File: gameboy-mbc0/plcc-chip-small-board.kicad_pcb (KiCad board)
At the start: 2 copper layers, 49.5 x 30.8 mm, 2 parts, among them P1 CONN_01X32, U1 SST39SF010

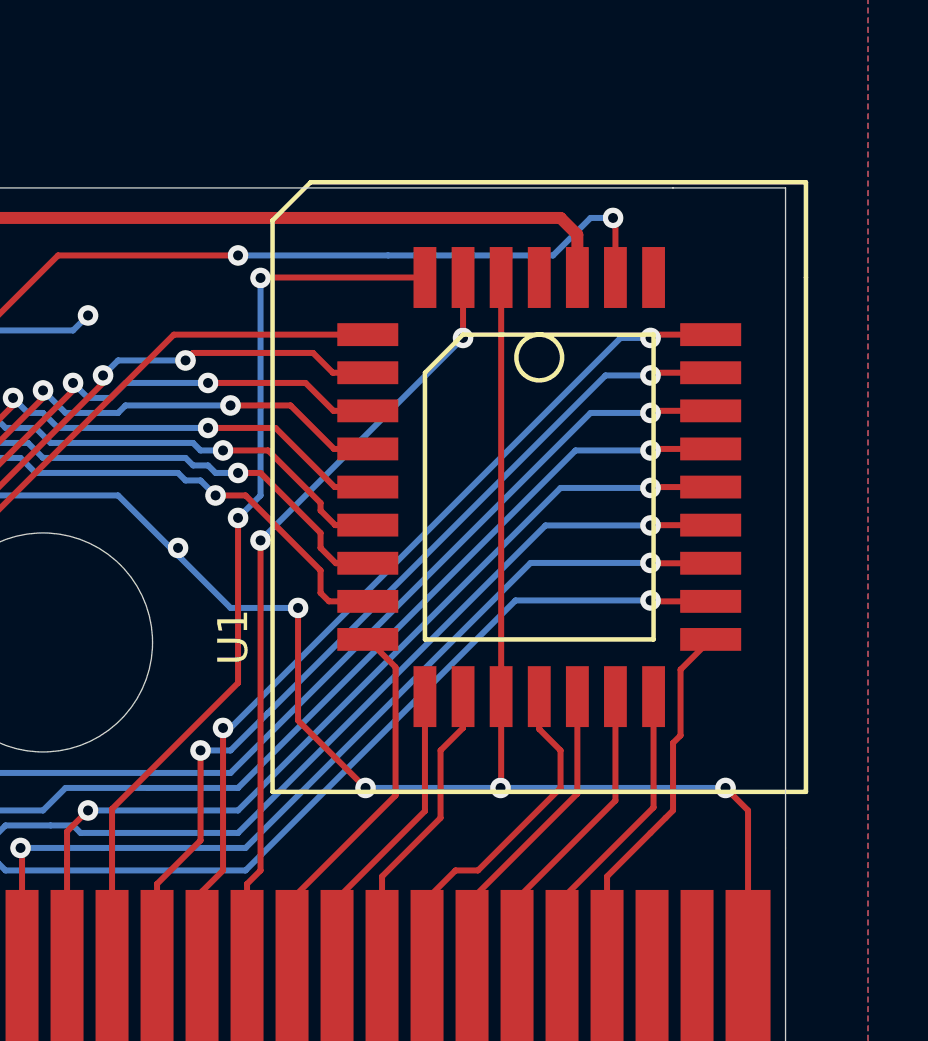
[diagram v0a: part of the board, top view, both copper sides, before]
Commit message: moved chip to avoid cartridge case
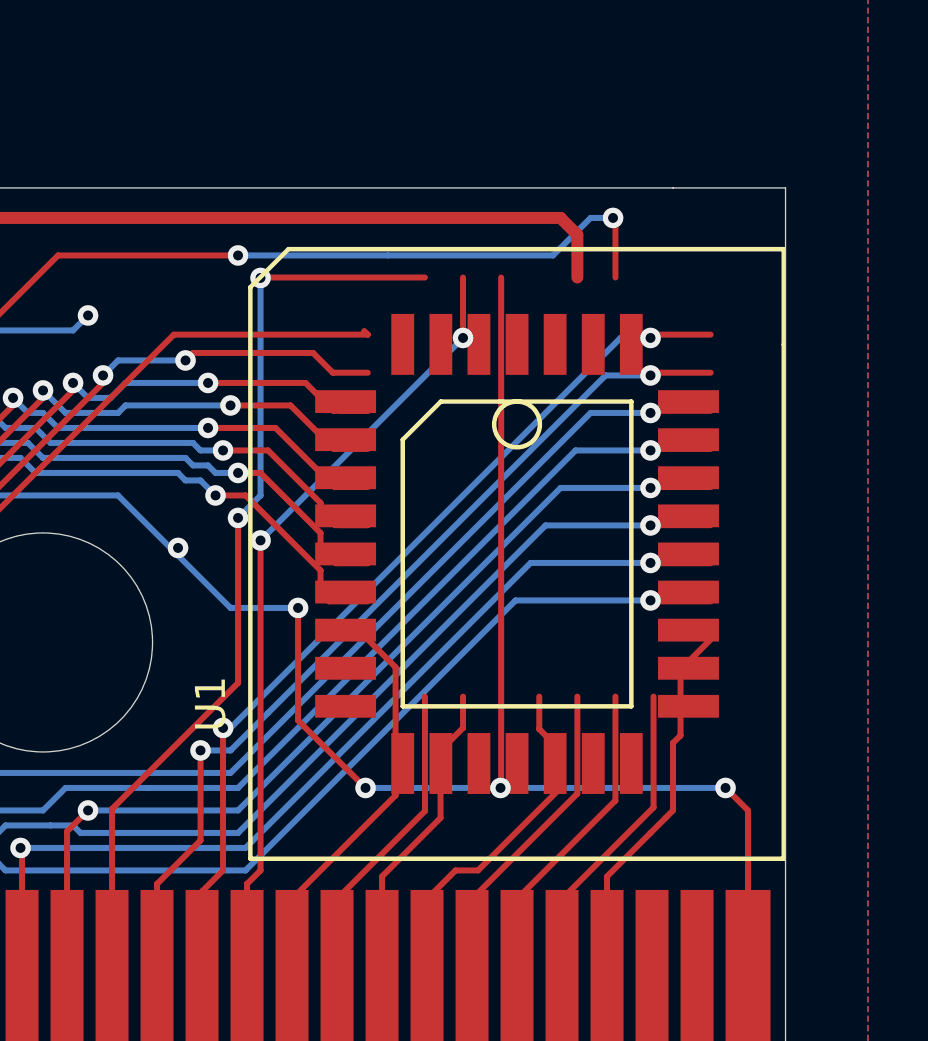
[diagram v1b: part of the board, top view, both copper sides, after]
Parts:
- moved U1 2.35 mm to (192.3, 143.2)
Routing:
- net Net-(P1-Pad6): track 41.8 -> 7.20 mm, vias 2 -> 0
- net Net-(P1-Pad7): track 40.3 -> 13.5 mm, vias 2 -> 0
- net Net-(P1-Pad12): track 33.7 -> 59.5 mm, vias 2 -> 4
- net Net-(P1-Pad5): track 47.8 -> 25.3 mm, vias 2 -> 1
- net Net-(P1-Pad11): track 35.7 -> 56.9 mm, vias 2 -> 4
- net Net-(P1-Pad19): track 31.0 -> 51.4 mm, vias 2 -> 3
- net Net-(P1-Pad16): track 31.9 -> 13.8 mm, vias 2 -> 1
- net Net-(P1-Pad14): track 38.4 -> 54.6 mm
- net Net-(P1-Pad25): track 12.5 -> 5.29 mm
- net Net-(P1-Pad26): track 11.4 -> 18.6 mm
- net Net-(P1-Pad13): track 32.6 -> 39.2 mm
- net Net-(P1-Pad29): track 16.5 -> 9.91 mm
- net Net-(P1-Pad22): track 13.7 -> 8.08 mm
- net Net-(P1-Pad15): track 35.4 -> 40.5 mm
- net Net-(P1-Pad10): track 36.0 -> 41.2 mm
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
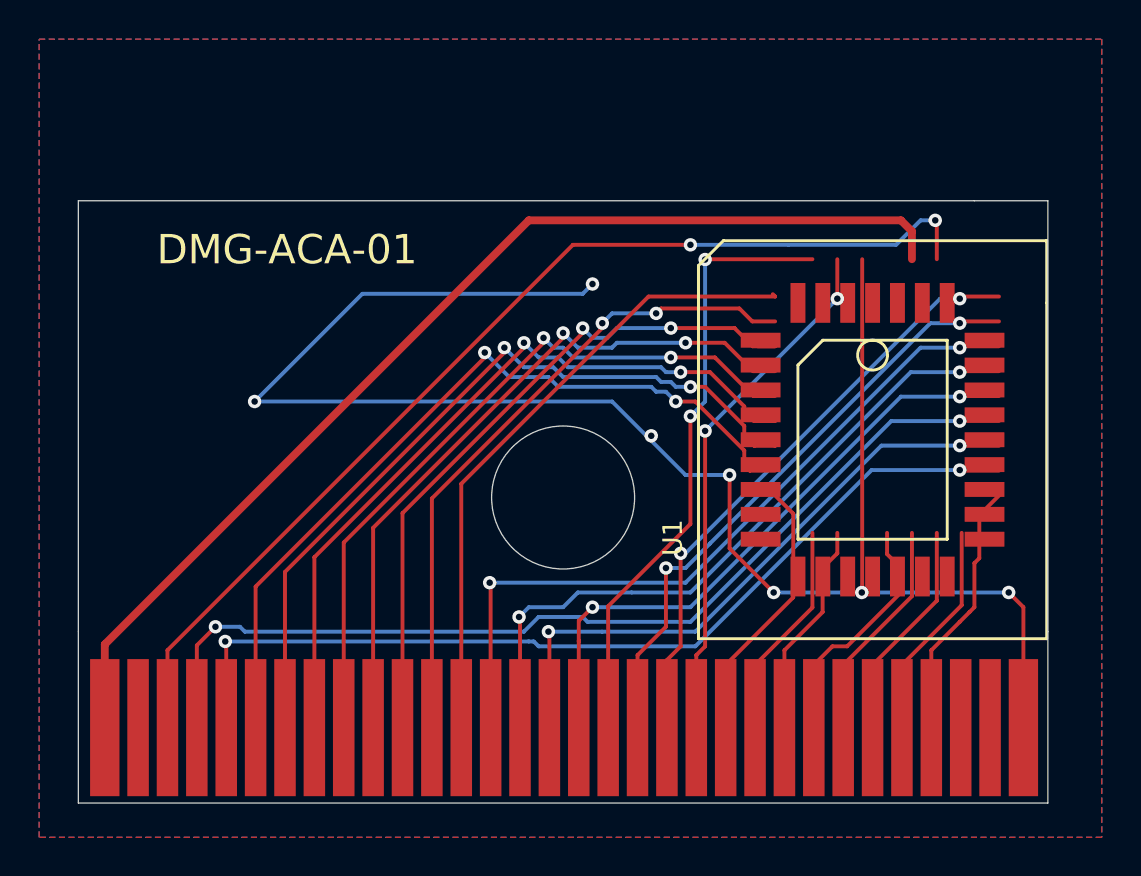
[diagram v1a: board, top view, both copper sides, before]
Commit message: successfully rerouted connections and made board smaller
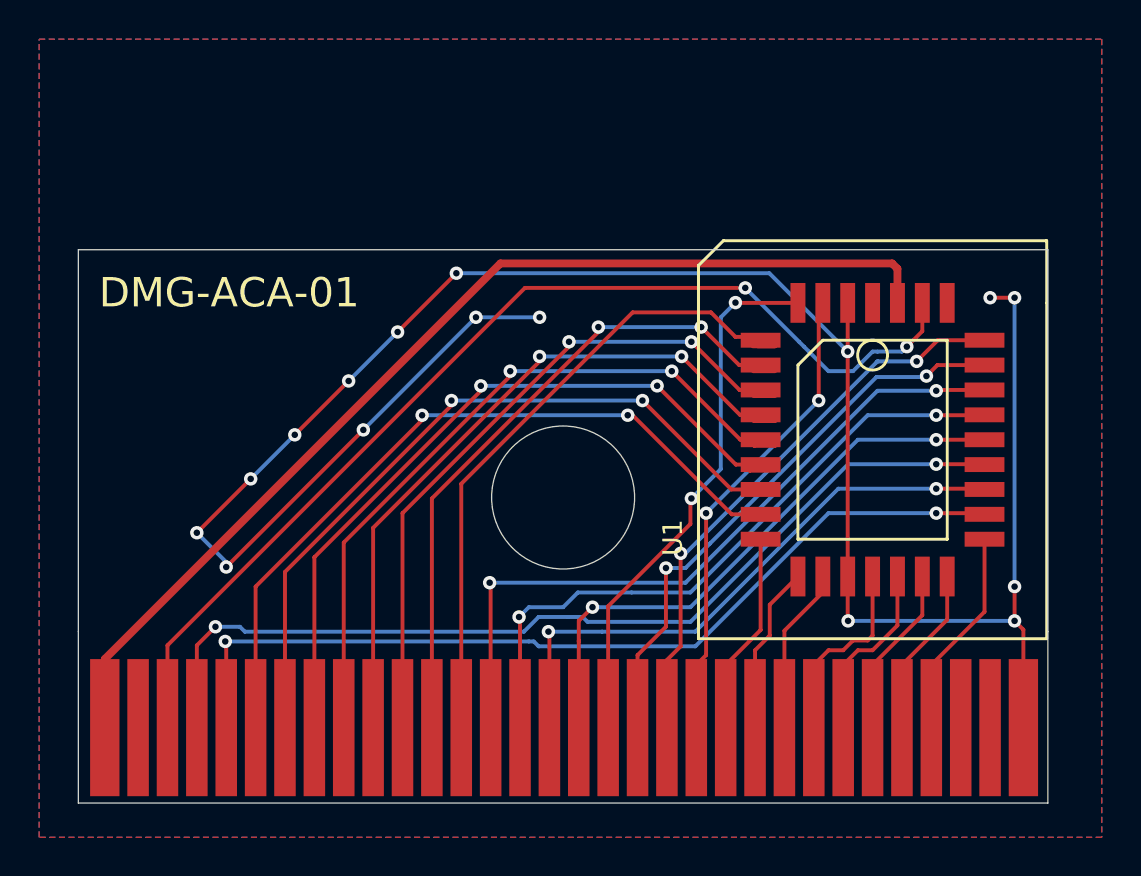
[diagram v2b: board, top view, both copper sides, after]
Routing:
- net Net-(P1-Pad6): track 7.20 -> 38.9 mm, vias 0 -> 2
- net Net-(P1-Pad12): track 59.5 -> 34.2 mm, vias 4 -> 2
- net Net-(P1-Pad7): track 13.5 -> 37.9 mm, vias 0 -> 2
- net GND: track 88.9 -> 112.2 mm, vias 7 -> 16
- net Net-(P1-Pad19): track 51.4 -> 29.3 mm, vias 3 -> 2
- net Net-(P1-Pad11): track 56.9 -> 35.1 mm, vias 4 -> 2
- net Net-(P1-Pad5): track 25.3 -> 46.2 mm, vias 1 -> 2
- net Net-(P1-Pad14): track 54.6 -> 36.8 mm
- net Net-(P1-Pad16): track 13.8 -> 30.2 mm, vias 1 -> 2
- net Net-(P1-Pad26): track 18.6 -> 10.6 mm
- net Net-(P1-Pad15): track 40.5 -> 33.8 mm
- net Net-(P1-Pad20): track 35.0 -> 29.4 mm, vias 3 -> 2
- net Net-(P1-Pad22): track 8.08 -> 13.6 mm
- net Net-(P1-Pad13): track 39.2 -> 34.0 mm
- net Net-(P1-Pad8): track 43.3 -> 38.6 mm
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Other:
- board size 49.5 x 30.8 mm -> 49.5 x 28.2 mm
